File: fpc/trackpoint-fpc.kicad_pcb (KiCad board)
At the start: 2 copper layers, 15 x 13.7 mm, 2 parts

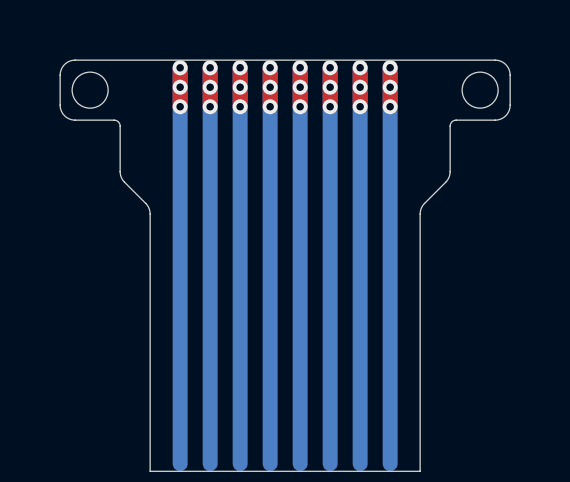
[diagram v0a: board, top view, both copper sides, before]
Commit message: Add silk screen text.
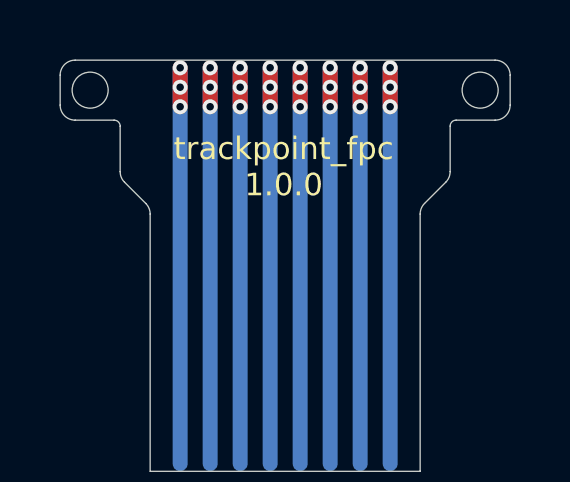
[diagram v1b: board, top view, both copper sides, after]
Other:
- board text added: "trackpoint_fpc 1.0.0"
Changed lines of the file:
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@@
   (general
     (thickness 1.6)
-    (drawings 59)
+    (drawings 60)
     (tracks 40)
     (zones 0)
@@
       (clearance 0.00001))
   )
+  (gr_text "trackpoint_fpc\n1.0.0" (at 212.95 138.2) (layer F.SilkS)
+    (effects (font (size 0.75 0.75) (thickness 0.15)))
+  )
   (gr_text "Stiffener TOP" (at 223.05 145.85) (layer Dwgs.User)

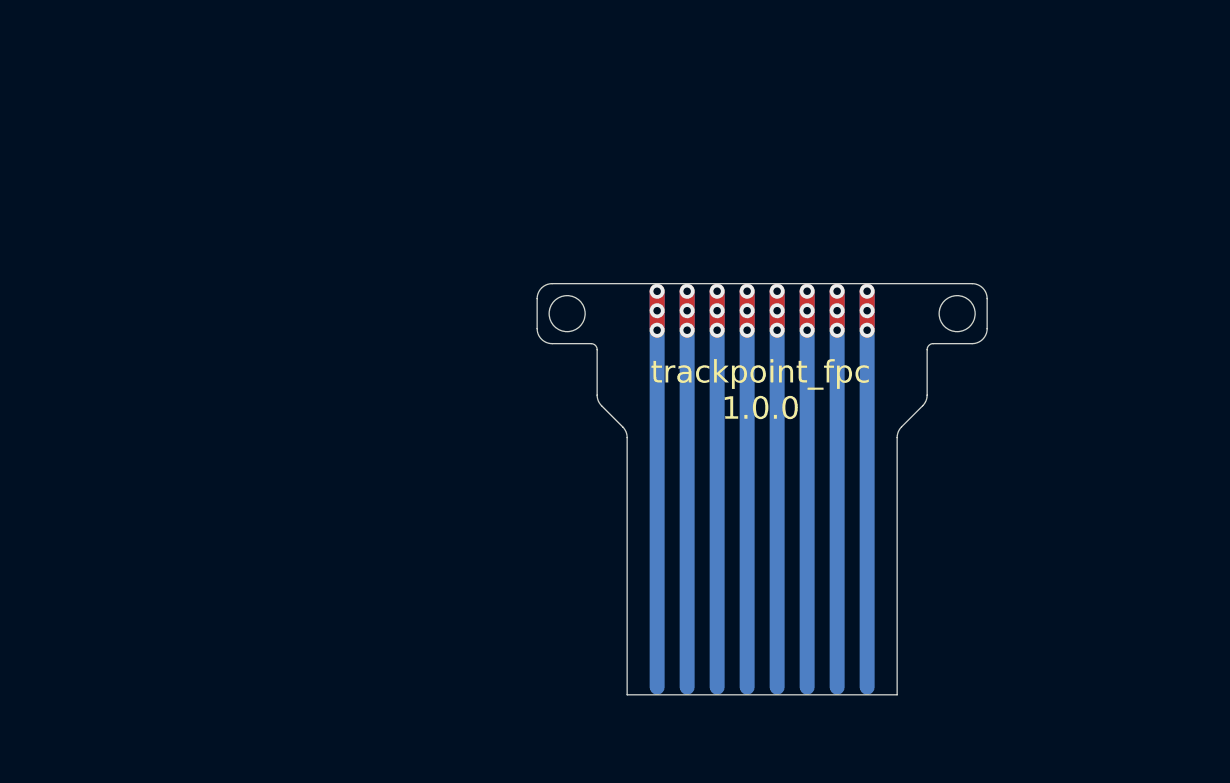
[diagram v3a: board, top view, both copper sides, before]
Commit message: Add new FPC.
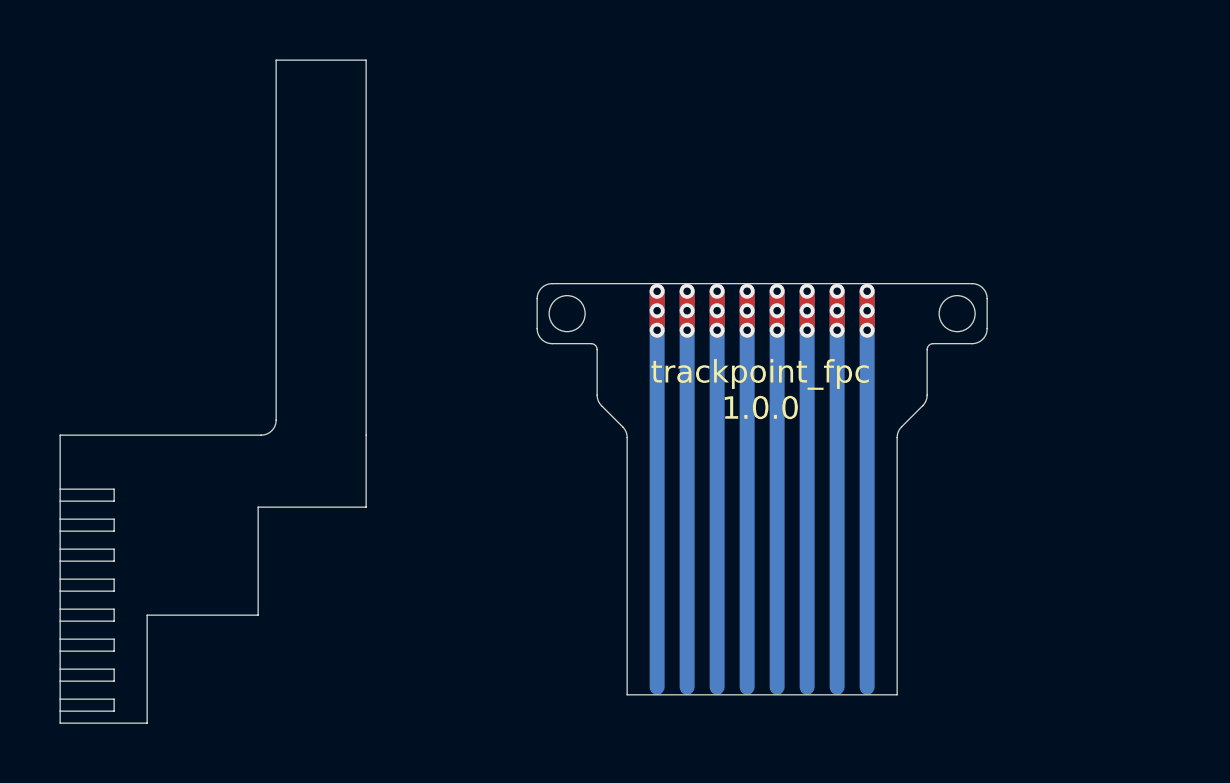
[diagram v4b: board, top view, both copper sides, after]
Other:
- board size 15 x 13.7 mm -> 30.9 x 22.1 mm
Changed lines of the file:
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@@
   (general
     (thickness 1.6)
-    (drawings 60)
+    (drawings 96)
     (tracks 40)
     (zones 0)
@@
   (gr_arc (start 207.3 136.847262) (end 207.5 136.847257) (angle -89.98075418) (layer Edge.Cuts) (width 0.01))
   (gr_arc (start 218.7 136.847262) (end 218.7 136.647257) (angle -90.00839267) (layer Edge.Cuts) (width 0.01))
+  (gr_line (start 189.6 147.8975) (end 191.4 147.8975) (angle 90) (layer Edge.Cuts) (width 0.01))
+  (gr_line (start 191.4 147.4975) (end 189.6 147.4975) (angle 90) (layer Edge.Cuts) (width 0.01))
+  (gr_line (start 191.4 147.8975) (end 191.4 147.4975) (angle 90) (layer Edge.Cuts) (width 0.01))
+  (gr_line (start 189.6 145.8975) (end 191.4 145.8975) (angle 90) (layer Edge.Cuts) (width 0.01))
+  (gr_line (start 191.4 145.4975) (end 189.6 145.4975) (angle 90) (layer Edge.Cuts) (width 0.01))
+  (gr_line (start 191.4 145.8975) (end 191.4 145.4975) (angle 90) (layer Edge.Cuts) (width 0.01))
+  (gr_line (start 189.6 143.8975) (end 191.4 143.8975) (angle 90) (layer Edge.Cuts) (width 0.01))
+  (gr_line (start 191.4 143.4975) (end 189.6 143.4975) (angle 90) (layer Edge.Cuts) (width 0.01))
+  (gr_line (start 191.4 143.8975) (end 191.4 143.4975) (angle 90) (layer Edge.Cuts) (width 0.01))
+  (gr_line (start 189.6 141.8975) (end 191.4 141.8975) (angle 90) (layer Edge.Cuts) (width 0.01))
+  (gr_line (start 191.4 141.4975) (end 189.6 141.4975) (angle 90) (layer Edge.Cuts) (width 0.01))
+  (gr_line (start 191.4 141.8975) (end 191.4 141.4975) (angle 90) (layer Edge.Cuts) (width 0.01))
+  (gr_line (start 189.6 142.8975) (end 191.4 142.8975) (angle 90) (layer Edge.Cuts) (width 0.01))
+  (gr_line (start 191.4 142.4975) (end 189.6 142.4975) (angle 90) (layer Edge.Cuts) (width 0.01))
+  (gr_line (start 191.4 142.8975) (end 191.4 142.4975) (angle 90) (layer Edge.Cuts) (width 0.01))
+  (gr_line (start 189.6 144.8975) (end 191.4 144.8975) (angle 90) (layer Edge.Cuts) (width 0.01))
+  (gr_line (start 191.4 144.4975) (end 189.6 144.4975) (angle 90) (layer Edge.Cuts) (width 0.01))
+  (gr_line (start 191.4 144.8975) (end 191.4 144.4975) (angle 90) (layer Edge.Cuts) (width 0.01))
+  (gr_line (start 189.6 146.8975) (end 191.4 146.8975) (angle 90) (layer Edge.Cuts) (width 0.01))
+  (gr_line (start 191.4 146.4975) (end 189.6 146.4975) (angle 90) (layer Edge.Cuts) (width 0.01))
+  (gr_line (start 191.4 146.8975) (end 191.4 146.4975) (angle 90) (layer Edge.Cuts) (width 0.01))
+  (gr_line (start 189.6 148.8975) (end 191.4 148.8975) (angle 90) (layer Edge.Cuts) (width 0.01))
+  (gr_line (start 191.4 148.4975) (end 189.6 148.4975) (angle 90) (layer Edge.Cuts) (width 0.01))
+  (gr_line (start 191.4 148.8975) (end 191.4 148.4975) (angle 90) (layer Edge.Cuts) (width 0.01))
+  (gr_line (start 199.8 127.1975) (end 199.8 139.6975) (angle 90) (layer Edge.Cuts) (width 0.01))
+  (gr_line (start 196.8 127.1975) (end 196.8 139.1975) (angle 90) (layer Edge.Cuts) (width 0.01))
+  (gr_line (start 196.3 139.6975) (end 189.6 139.6975) (angle 90) (layer Edge.Cuts) (width 0.01))
+  (gr_line (start 192.5 149.2975) (end 192.5 145.6975) (angle 90) (layer Edge.Cuts) (width 0.01))
+  (gr_line (start 189.6 149.2975) (end 192.5 149.2975) (angle 90) (layer Edge.Cuts) (width 0.01))
+  (gr_line (start 189.6 139.6975) (end 189.6 149.2975) (angle 90) (layer Edge.Cuts) (width 0.01))
+  (gr_line (start 196.2 145.6975) (end 196.2 142.0975) (angle 90) (layer Edge.Cuts) (width 0.01))
+  (gr_line (start 192.5 145.6975) (end 196.2 145.6975) (angle 90) (layer Edge.Cuts) (width 0.01))
+  (gr_line (start 199.8 142.0975) (end 199.8 139.6975) (angle 90) (layer Edge.Cuts) (width 0.01))
+  (gr_line (start 196.2 142.0975) (end 199.8 142.0975) (angle 90) (layer Edge.Cuts) (width 0.01))
+  (gr_line (start 199.8 127.1975) (end 196.8 127.1975) (angle 90) (layer Edge.Cuts) (width 0.01))
+  (gr_arc (start 196.300006 139.197511) (end 196.3 139.6975) (angle -90.00254177) (layer Edge.Cuts) (width 0.01))
   (segment (start 210.5 134.9) (end 210.5 148.1) (width 0.5) (layer B.Cu) (net 0))
   (segment (start 211.5 134.9) (end 211.5 148.1) (width 0.5) (layer B.Cu) (net 0))

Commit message: Add pad tracks for the new FPC.
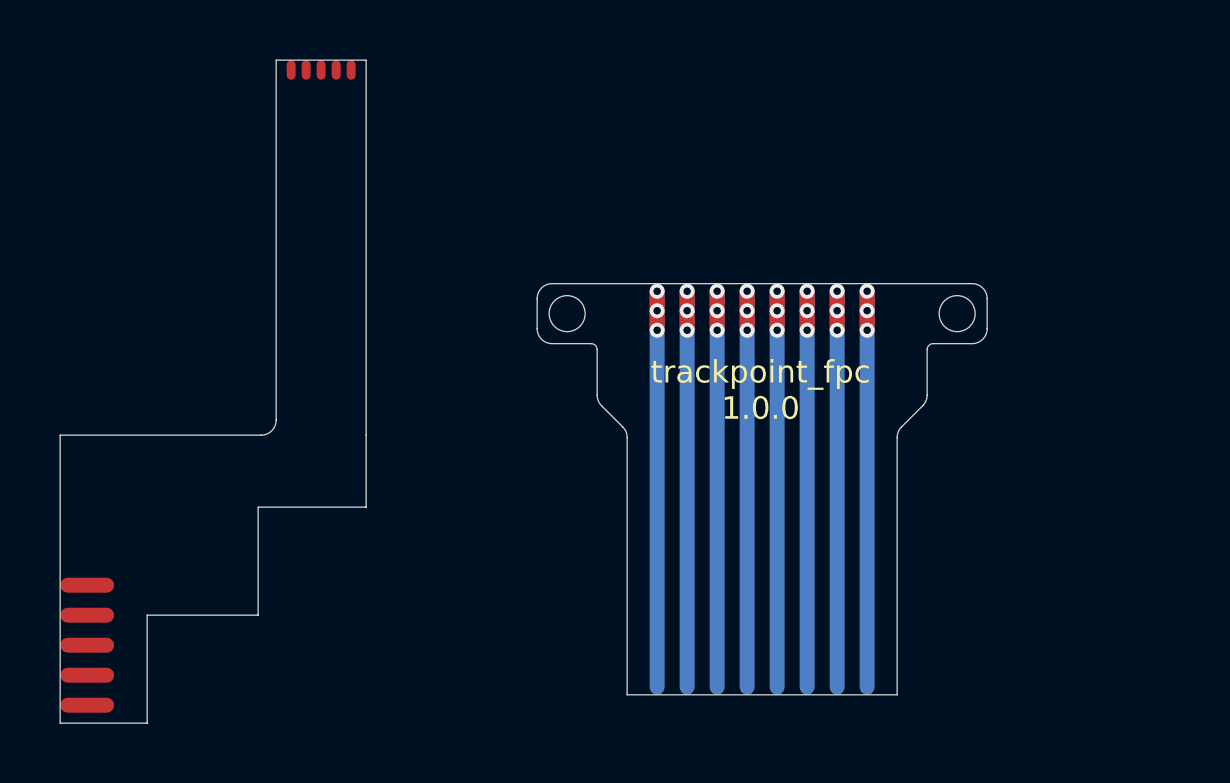
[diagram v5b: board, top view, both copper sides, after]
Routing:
- net (no net): track 116.0 -> 124.2 mm
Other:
- outline, holes or cut-outs redrawn
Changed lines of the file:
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@@
     (thickness 1.6)
     (drawings 96)
-    (tracks 40)
+    (tracks 50)
     (zones 0)
     (modules 2)
@@
   )
   (setup
-    (last_trace_width 0.5)
+    (last_trace_width 0.3)
+    (user_trace_width 0.3)
     (trace_clearance 0)
     (zone_clearance 0.508)
@@
   (gr_arc (start 207.3 136.847262) (end 207.5 136.847257) (angle -89.98075418) (layer Edge.Cuts) (width 0.01))
   (gr_arc (start 218.7 136.847262) (end 218.7 136.647257) (angle -90.00839267) (layer Edge.Cuts) (width 0.01))
-  (gr_line (start 189.6 147.8975) (end 191.4 147.8975) (angle 90) (layer Edge.Cuts) (width 0.01))
-  (gr_line (start 191.4 147.4975) (end 189.6 147.4975) (angle 90) (layer Edge.Cuts) (width 0.01))
-  (gr_line (start 191.4 147.8975) (end 191.4 147.4975) (angle 90) (layer Edge.Cuts) (width 0.01))
-  (gr_line (start 189.6 145.8975) (end 191.4 145.8975) (angle 90) (layer Edge.Cuts) (width 0.01))
-  (gr_line (start 191.4 145.4975) (end 189.6 145.4975) (angle 90) (layer Edge.Cuts) (width 0.01))
-  (gr_line (start 191.4 145.8975) (end 191.4 145.4975) (angle 90) (layer Edge.Cuts) (width 0.01))
-  (gr_line (start 189.6 143.8975) (end 191.4 143.8975) (angle 90) (layer Edge.Cuts) (width 0.01))
-  (gr_line (start 191.4 143.4975) (end 189.6 143.4975) (angle 90) (layer Edge.Cuts) (width 0.01))
-  (gr_line (start 191.4 143.8975) (end 191.4 143.4975) (angle 90) (layer Edge.Cuts) (width 0.01))
-  (gr_line (start 189.6 141.8975) (end 191.4 141.8975) (angle 90) (layer Edge.Cuts) (width 0.01))
-  (gr_line (start 191.4 141.4975) (end 189.6 141.4975) (angle 90) (layer Edge.Cuts) (width 0.01))
-  (gr_line (start 191.4 141.8975) (end 191.4 141.4975) (angle 90) (layer Edge.Cuts) (width 0.01))
-  (gr_line (start 189.6 142.8975) (end 191.4 142.8975) (angle 90) (layer Edge.Cuts) (width 0.01))
-  (gr_line (start 191.4 142.4975) (end 189.6 142.4975) (angle 90) (layer Edge.Cuts) (width 0.01))
-  (gr_line (start 191.4 142.8975) (end 191.4 142.4975) (angle 90) (layer Edge.Cuts) (width 0.01))
-  (gr_line (start 189.6 144.8975) (end 191.4 144.8975) (angle 90) (layer Edge.Cuts) (width 0.01))
-  (gr_line (start 191.4 144.4975) (end 189.6 144.4975) (angle 90) (layer Edge.Cuts) (width 0.01))
-  (gr_line (start 191.4 144.8975) (end 191.4 144.4975) (angle 90) (layer Edge.Cuts) (width 0.01))
-  (gr_line (start 189.6 146.8975) (end 191.4 146.8975) (angle 90) (layer Edge.Cuts) (width 0.01))
-  (gr_line (start 191.4 146.4975) (end 189.6 146.4975) (angle 90) (layer Edge.Cuts) (width 0.01))
-  (gr_line (start 191.4 146.8975) (end 191.4 146.4975) (angle 90) (layer Edge.Cuts) (width 0.01))
-  (gr_line (start 189.6 148.8975) (end 191.4 148.8975) (angle 90) (layer Edge.Cuts) (width 0.01))
-  (gr_line (start 191.4 148.4975) (end 189.6 148.4975) (angle 90) (layer Edge.Cuts) (width 0.01))
-  (gr_line (start 191.4 148.8975) (end 191.4 148.4975) (angle 90) (layer Edge.Cuts) (width 0.01))
+  (gr_line (start 189.6 147.8975) (end 191.4 147.8975) (angle 90) (layer Cmts.User) (width 0.01))
+  (gr_line (start 191.4 147.4975) (end 189.6 147.4975) (angle 90) (layer Cmts.User) (width 0.01))
+  (gr_line (start 191.4 147.8975) (end 191.4 147.4975) (angle 90) (layer Cmts.User) (width 0.01))
+  (gr_line (start 189.6 145.8975) (end 191.4 145.8975) (angle 90) (layer Cmts.User) (width 0.01))
+  (gr_line (start 191.4 145.4975) (end 189.6 145.4975) (angle 90) (layer Cmts.User) (width 0.01))
+  (gr_line (start 191.4 145.8975) (end 191.4 145.4975) (angle 90) (layer Cmts.User) (width 0.01))
+  (gr_line (start 189.6 143.8975) (end 191.4 143.8975) (angle 90) (layer Cmts.User) (width 0.01))
+  (gr_line (start 191.4 143.4975) (end 189.6 143.4975) (angle 90) (layer Cmts.User) (width 0.01))
+  (gr_line (start 191.4 143.8975) (end 191.4 143.4975) (angle 90) (layer Cmts.User) (width 0.01))
+  (gr_line (start 189.6 141.8975) (end 191.4 141.8975) (angle 90) (layer Cmts.User) (width 0.01))
+  (gr_line (start 191.4 141.4975) (end 189.6 141.4975) (angle 90) (layer Cmts.User) (width 0.01))
+  (gr_line (start 191.4 141.8975) (end 191.4 141.4975) (angle 90) (layer Cmts.User) (width 0.01))
+  (gr_line (start 189.6 142.8975) (end 191.4 142.8975) (angle 90) (layer Cmts.User) (width 0.01))
+  (gr_line (start 191.4 142.4975) (end 189.6 142.4975) (angle 90) (layer Cmts.User) (width 0.01))
+  (gr_line (start 191.4 142.8975) (end 191.4 142.4975) (angle 90) (layer Cmts.User) (width 0.01))
+  (gr_line (start 189.6 144.8975) (end 191.4 144.8975) (angle 90) (layer Cmts.User) (width 0.01))
+  (gr_line (start 191.4 144.4975) (end 189.6 144.4975) (angle 90) (layer Cmts.User) (width 0.01))
+  (gr_line (start 191.4 144.8975) (end 191.4 144.4975) (angle 90) (layer Cmts.User) (width 0.01))
+  (gr_line (start 189.6 146.8975) (end 191.4 146.8975) (angle 90) (layer Cmts.User) (width 0.01))
+  (gr_line (start 191.4 146.4975) (end 189.6 146.4975) (angle 90) (layer Cmts.User) (width 0.01))
+  (gr_line (start 191.4 146.8975) (end 191.4 146.4975) (angle 90) (layer Cmts.User) (width 0.01))
+  (gr_line (start 189.6 148.8975) (end 191.4 148.8975) (angle 90) (layer Cmts.User) (width 0.01))
+  (gr_line (start 191.4 148.4975) (end 189.6 148.4975) (angle 90) (layer Cmts.User) (width 0.01))
+  (gr_line (start 191.4 148.8975) (end 191.4 148.4975) (angle 90) (layer Cmts.User) (width 0.01))
   (gr_line (start 199.8 127.1975) (end 199.8 139.6975) (angle 90) (layer Edge.Cuts) (width 0.01))
   (gr_line (start 196.8 127.1975) (end 196.8 139.1975) (angle 90) (layer Edge.Cuts) (width 0.01))
@@
   (segment (start 215.5 136.2) (end 215.5 134.902267) (width 0.5) (layer F.Cu) (net 0))
   (segment (start 216.5 136.2) (end 216.5 134.902267) (width 0.5) (layer F.Cu) (net 0))
+  (segment (start 191.15 144.7) (end 189.85501 144.7) (width 0.5) (layer F.Cu) (net 0))
+  (segment (start 191.15 145.7) (end 189.85501 145.7) (width 0.5) (layer F.Cu) (net 0))
+  (segment (start 191.15 146.7) (end 189.85501 146.7) (width 0.5) (layer F.Cu) (net 0))
+  (segment (start 191.15 147.7) (end 189.85501 147.7) (width 0.5) (layer F.Cu) (net 0))
+  (segment (start 191.15 148.7) (end 189.85501 148.7) (width 0.5) (layer F.Cu) (net 0))
+  (segment (start 198.3 127.7) (end 198.3 127.35251) (width 0.3) (layer F.Cu) (net 0))
+  (segment (start 199.3 127.7) (end 199.3 127.35251) (width 0.3) (layer F.Cu) (net 0))
+  (segment (start 197.8 127.7) (end 197.8 127.35251) (width 0.3) (layer F.Cu) (net 0))
+  (segment (start 197.3 127.7) (end 197.3 127.35251) (width 0.3) (layer F.Cu) (net 0))
+  (segment (start 198.8 127.7) (end 198.8 127.35251) (width 0.3) (layer F.Cu) (net 0))
 )
